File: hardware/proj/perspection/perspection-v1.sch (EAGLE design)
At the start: 273 parts, among them J1 MICRO-USB-10118192-0001LF, J10 1X5, J11 1X4, J2 1X6-PTSA_1.5/6-3.5-Z, J3 1X2-PTSA_1.5/2-3.5-Z, J4 1X2-JST-PH-SMD, J5 1X2-0428202213, J6 JTAG-ARM_TC-10, J7 JTAG-ARM_TC-10, J8 1X3-0.1IN_THRUHOLE, J9 1X2-PTSA_1.5/2-3.5-Z, Q1 NMOS-CSD18533Q5A, Q10 NMOS-CSD18533Q5A, Q11 IRFML8244TRPBF, Q2 NMOS-CSD18533Q5A, Q3 NMOS-CSD18533Q5A, Q4 NMOS-CSD18533Q5A, Q5 NMOS-CSD18533Q5A, Q6 NMOS-CSD18533Q5A, Q7 NMOS-CSD18533Q5A, Q8 BSS138L, Q9 BSS138L, U1 ATUM, U10 DRV8301DCAR, U11 OPA2374AIDCNR, U12 OPA170AIDBVR, U13 BNO055, U14 TPS81256, U2 FT232RQ, U3 TPS79933DDCR, U4 MCP73831T-2ACI/OT, U5 TMS320F28069MPZT, U6 DRV8801PWPR, U7 DRV8801PWPR, U8 DRV8801PWPR, U9 DRV8801PWPR, Y1 32.768kHz

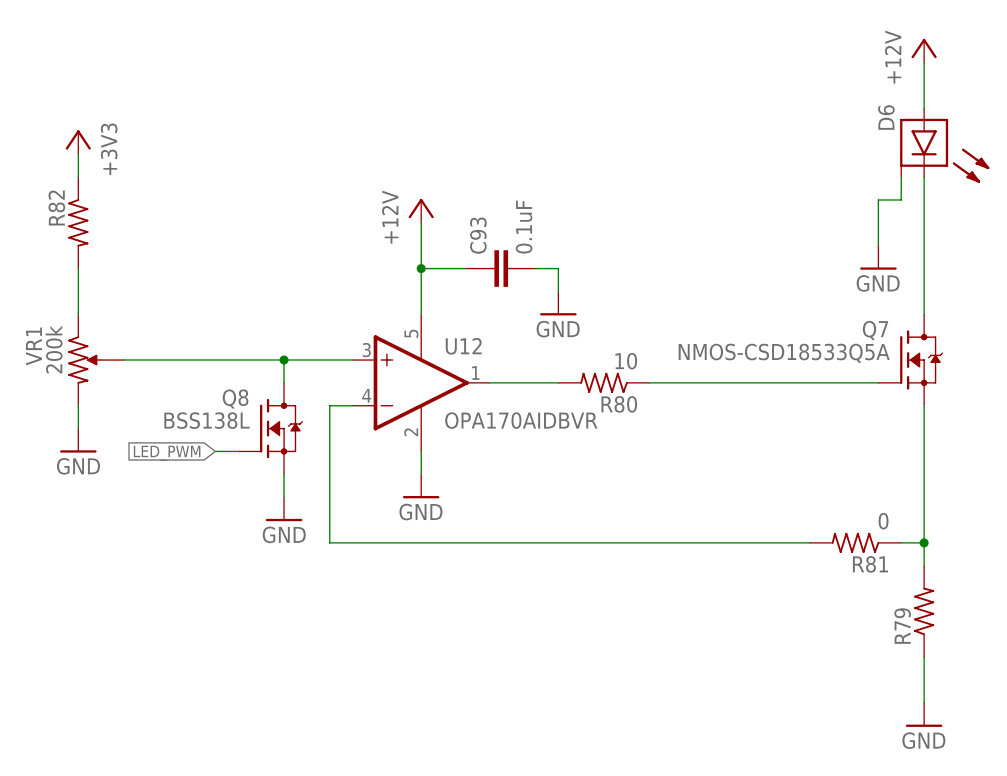
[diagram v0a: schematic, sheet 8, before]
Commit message: fixed stub (!!), set resistor values for LED driver and updated part numbers accordingly
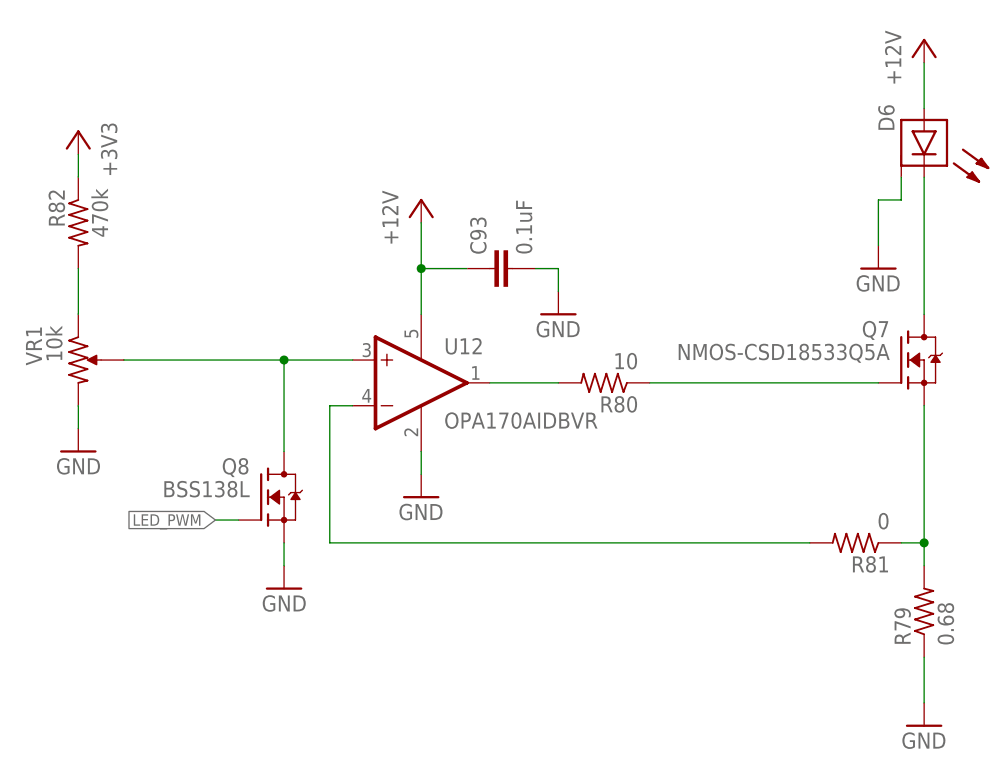
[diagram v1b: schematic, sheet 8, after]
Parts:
- R79: value (none) -> 0.68
- R82: value (none) -> 470k
- VR1: value 200k -> 10k
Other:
- moved on the sheet: Q8
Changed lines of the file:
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@@
 <part name="Q7" library="perspection" deviceset="NMOS" device="-CSD18533Q5A"/>
 <part name="D6" library="perspection" deviceset="LED-PWR" device="-XLAMP_MX3"/>
-<part name="R79" library="perspection" deviceset="R" device="0805"/>
+<part name="R79" library="perspection" deviceset="R" device="0805" value="0.68"/>
 <part name="GND64" library="perspection" deviceset="GND" device=""/>
 <part name="R80" library="perspection" deviceset="R" device="0402" value="10"/>
 <part name="U12" library="perspection" deviceset="OPA170" device="AIDBVR"/>
 <part name="R81" library="perspection" deviceset="R" device="0402" value="0"/>
-<part name="R82" library="perspection" deviceset="R" device="0402"/>
-<part name="VR1" library="perspection" deviceset="R-TRIM" device="-ST4ETA204" value="200k"/>
+<part name="R82" library="perspection" deviceset="R" device="0402" value="470k"/>
+<part name="VR1" library="perspection" deviceset="R-TRIM" device="-ST4ETA204" value="10k"/>
 <part name="GND65" library="perspection" deviceset="GND" device=""/>
 <part name="C82" library="perspection" deviceset="CPOL" device="-PANASONIC-6.3MM-SMD-220UF-25V" value="220uF">
@@
 <instance part="VR1" gate="G$1" x="144.78" y="144.78" rot="MR270"/>
 <instance part="GND65" gate="1" x="144.78" y="134.62" rot="MR0"/>
-<instance part="Q8" gate="G$1" x="165.1" y="137.16"/>
+<instance part="Q8" gate="G$1" x="165.1" y="129.54"/>
 <instance part="+3V21" gate="G$1" x="144.78" y="170.18" rot="MR0"/>
 <instance part="GND73" gate="1" x="182.88" y="129.54"/>
@@
 <instance part="GND74" gate="1" x="198.12" y="149.86"/>
 <instance part="P+15" gate="G$1" x="238.76" y="177.8"/>
-<instance part="GND76" gate="1" x="167.64" y="127" rot="MR0"/>
+<instance part="GND76" gate="1" x="167.64" y="119.38" rot="MR0"/>
 <instance part="GND83" gate="1" x="233.68" y="154.94"/>
 </instances>
@@
 <segment>
 <pinref part="Q8" gate="G$1" pin="S"/>
-<wire x1="167.64" y1="129.54" x2="167.64" y2="132.08" width="0.1524" layer="91"/>
+<wire x1="167.64" y1="121.92" x2="167.64" y2="124.46" width="0.1524" layer="91"/>
 <pinref part="GND76" gate="1" pin="GND"/>
 </segment>
@@
 <pinref part="Q8" gate="G$1" pin="D"/>
 <wire x1="149.86" y1="144.78" x2="167.64" y2="144.78" width="0.1524" layer="91"/>
-<wire x1="167.64" y1="144.78" x2="167.64" y2="142.24" width="0.1524" layer="91"/>
+<wire x1="167.64" y1="144.78" x2="167.64" y2="134.62" width="0.1524" layer="91"/>
 <junction x="167.64" y="144.78"/>
 <pinref part="U12" gate="G$1" pin="+IN"/>
@@
 <segment>
 <pinref part="Q8" gate="G$1" pin="G"/>
-<wire x1="162.56" y1="134.62" x2="160.02" y2="134.62" width="0.1524" layer="91"/>
-<label x="160.02" y="134.62" size="1.27" layer="95" rot="R180" xref="yes"/>
+<wire x1="162.56" y1="127" x2="160.02" y2="127" width="0.1524" layer="91"/>
+<label x="160.02" y="127" size="1.27" layer="95" rot="R180" xref="yes"/>
 </segment>
 </net>
